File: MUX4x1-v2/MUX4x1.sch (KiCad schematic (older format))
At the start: 14 parts, among them J1 Screw_Terminal_01x02, J2 Conn_01x09_Male, J3 Conn_01x09_Male, J4 Conn_01x09_Male, J5 Conn_01x09_Male, J6 Conn_01x09_Male, J7 Conn_01x03_Male, U1 74LS153, U2 74LS153, U3 74LS153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

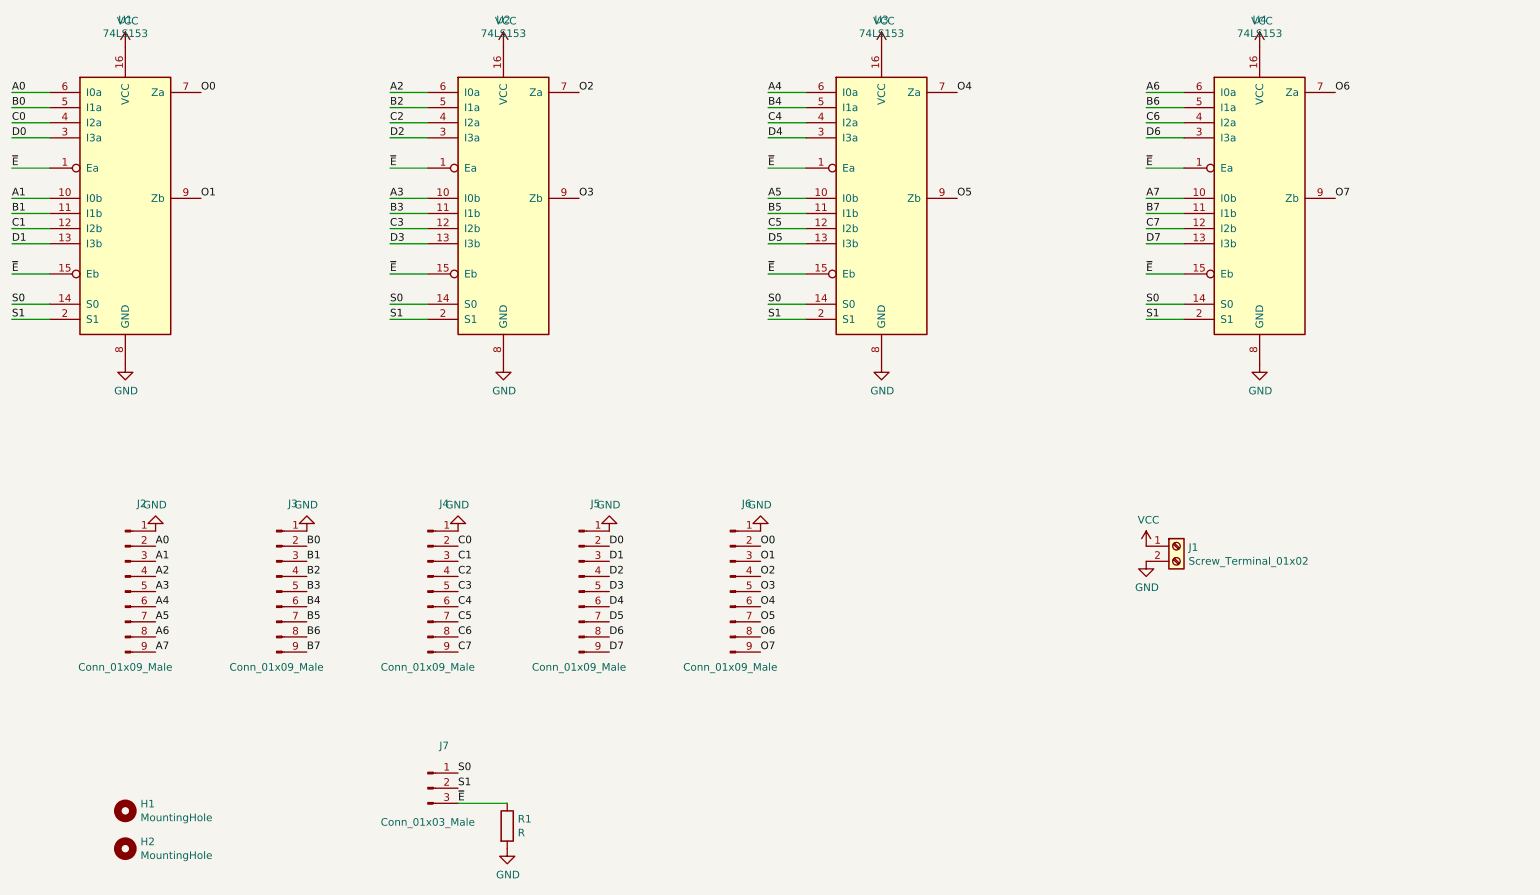
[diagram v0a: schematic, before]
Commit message: We need more sockets!!
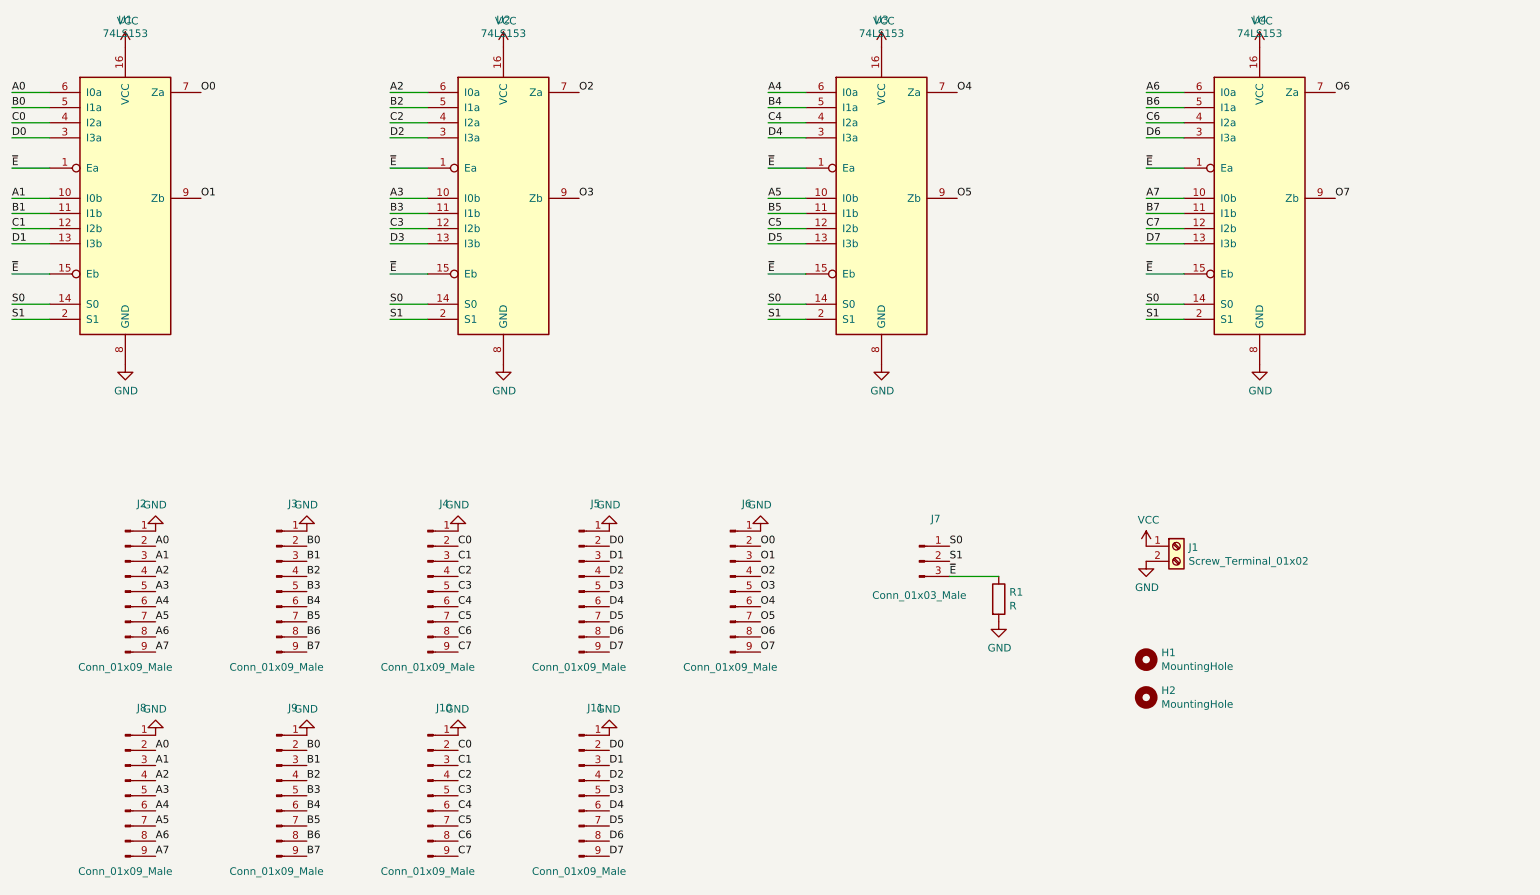
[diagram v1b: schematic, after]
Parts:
- added J10, J11, J8, J9: Conn_01x09_Male, Connector_PinHeader_2.54mm:PinHeader_1x09_P2.54mm_Vertical, symbol Connector:Conn_01x09_Male
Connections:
- net A0: now also J8.2 (Pin_2)
- net A1: now also J8.3 (Pin_3)
- net A2: now also J8.4 (Pin_4)
- net A3: now also J8.5 (Pin_5)
- net A4: now also J8.6 (Pin_6)
- net A5: now also J8.7 (Pin_7)
- net A6: now also J8.8 (Pin_8)
- net A7: now also J8.9 (Pin_9)
- net B0: now also J9.2 (Pin_2)
- net B1: now also J9.3 (Pin_3)
- net B2: now also J9.4 (Pin_4)
- net B3: now also J9.5 (Pin_5)
- net B4: now also J9.6 (Pin_6)
- net B5: now also J9.7 (Pin_7)
- net B6: now also J9.8 (Pin_8)
- net B7: now also J9.9 (Pin_9)
- net C0: now also J10.2 (Pin_2)
- net C1: now also J10.3 (Pin_3)
- net C2: now also J10.4 (Pin_4)
- net C3: now also J10.5 (Pin_5)
- net C4: now also J10.6 (Pin_6)
- net C5: now also J10.7 (Pin_7)
- net C6: now also J10.8 (Pin_8)
- net C7: now also J10.9 (Pin_9)
- net D0: now also J11.2 (Pin_2)
- net D1: now also J11.3 (Pin_3)
- net D2: now also J11.4 (Pin_4)
- net D3: now also J11.5 (Pin_5)
- net D4: now also J11.6 (Pin_6)
- net D5: now also J11.7 (Pin_7)
- net D6: now also J11.8 (Pin_8)
- net D7: now also J11.9 (Pin_9)
- net GND: now also J10.1 (Pin_1), J11.1 (Pin_1), J8.1 (Pin_1), J9.1 (Pin_1)
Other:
- moved on the sheet: H1, H2, J7, R1
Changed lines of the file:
@@
 L Mechanical:MountingHole H1
 U 1 1 62E202A1
-P 2000 6750
-F 0 "H1" H 2100 6796 50  0000 L CNN
-F 1 "MountingHole" H 2100 6705 50  0000 L CNN
-F 2 "MountingHole:MountingHole_3.2mm_M3" H 2000 6750 50  0001 C CNN
-F 3 "~" H 2000 6750 50  0001 C CNN
-	1    2000 6750
+P 8750 5750
+F 0 "H1" H 8850 5796 50  0000 L CNN
+F 1 "MountingHole" H 8850 5705 50  0000 L CNN
+F 2 "MountingHole:MountingHole_3.2mm_M3" H 8750 5750 50  0001 C CNN
+F 3 "~" H 8750 5750 50  0001 C CNN
+	1    8750 5750
 	1    0    0    -1
 $EndComp
@@
 L Mechanical:MountingHole H2
 U 1 1 62E20901
-P 2000 7000
-F 0 "H2" H 2100 7046 50  0000 L CNN
-F 1 "MountingHole" H 2100 6955 50  0000 L CNN
-F 2 "MountingHole:MountingHole_3.2mm_M3" H 2000 7000 50  0001 C CNN
-F 3 "~" H 2000 7000 50  0001 C CNN
-	1    2000 7000
+P 8750 6000
+F 0 "H2" H 8850 6046 50  0000 L CNN
+F 1 "MountingHole" H 8850 5955 50  0000 L CNN
+F 2 "MountingHole:MountingHole_3.2mm_M3" H 8750 6000 50  0001 C CNN
+F 3 "~" H 8750 6000 50  0001 C CNN
+	1    8750 6000
 	1    0    0    -1
 $EndComp
@@
 L Connector:Conn_01x03_Male J7
 U 1 1 62E1D5C5
-P 4000 6600
-F 0 "J7" H 4108 6881 50  0000 C CNN
-F 1 "Conn_01x03_Male" H 4000 6375 50  0000 C CNN
-F 2 "Connector_PinHeader_2.54mm:PinHeader_1x03_P2.54mm_Vertical" H 4000 6600 50  0001 C CNN
-F 3 "~" H 4000 6600 50  0001 C CNN
-	1    4000 6600
-	1    0    0    -1
-$EndComp
-Text Label 4200 6500 0    50   ~ 0
+P 7250 5100
+F 0 "J7" H 7358 5381 50  0000 C CNN
+F 1 "Conn_01x03_Male" H 7250 4875 50  0000 C CNN
+F 2 "Connector_PinHeader_2.54mm:PinHeader_1x03_P2.54mm_Vertical" H 7250 5100 50  0001 C CNN
+F 3 "~" H 7250 5100 50  0001 C CNN
+	1    7250 5100
+	1    0    0    -1
+$EndComp
+Text Label 7450 5000 0    50   ~ 0
 S0
-Text Label 4200 6600 0    50   ~ 0
+Text Label 7450 5100 0    50   ~ 0
 S1
-Text Label 4200 6700 0    50   ~ 0
+Text Label 7450 5200 0    50   ~ 0
 ~E
 $Comp
 L Device:R R1
 U 1 1 62E1F3C7
-P 4525 6850
-F 0 "R1" H 4595 6896 50  0000 L CNN
-F 1 "R" H 4595 6805 50  0000 L CNN
-F 2 "Resistor_SMD:R_0805_2012Metric_Pad1.20x1.40mm_HandSolder" V 4455 6850 50  0001 C CNN
-F 3 "~" H 4525 6850 50  0001 C CNN
-	1    4525 6850
-	1    0    0    -1
-$EndComp
-Wire Wire Line
-	4200 6700 4525 6700
+P 7775 5350
+F 0 "R1" H 7845 5396 50  0000 L CNN
+F 1 "R" H 7845 5305 50  0000 L CNN
+F 2 "Resistor_SMD:R_0805_2012Metric_Pad1.20x1.40mm_HandSolder" V 7705 5350 50  0001 C CNN
+F 3 "~" H 7775 5350 50  0001 C CNN
+	1    7775 5350
+	1    0    0    -1
+$EndComp
+Wire Wire Line
+	7450 5200 7775 5200
 $Comp
 L power:GND #PWR016
 U 1 1 62E205E6
-P 4525 7000
-F 0 "#PWR016" H 4525 6750 50  0001 C CNN
-F 1 "GND" H 4530 6827 50  0000 C CNN
-F 2 "" H 4525 7000 50  0001 C CNN
-F 3 "" H 4525 7000 50  0001 C CNN
-	1    4525 7000
+P 7775 5500
+F 0 "#PWR016" H 7775 5250 50  0001 C CNN
+F 1 "GND" H 7780 5327 50  0000 C CNN
+F 2 "" H 7775 5500 50  0001 C CNN
+F 3 "" H 7775 5500 50  0001 C CNN
+	1    7775 5500
 	1    0    0    -1
 $EndComp
@@
 Text Label 1250 2500 0    50   ~ 0
 ~E
+$Comp
+L Connector:Conn_01x09_Male J8
+U 1 1 62E33207
+P 2000 6650
+F 0 "J8" H 2108 7231 50  0000 C CNN
+F 1 "Conn_01x09_Male" H 2000 6150 50  0000 C CNN
+F 2 "Connector_PinHeader_2.54mm:PinHeader_1x09_P2.54mm_Vertical" H 2000 6650 50  0001 C CNN
+F 3 "~" H 2000 6650 50  0001 C CNN
+	1    2000 6650
+	1    0    0    -1
+$EndComp
+$Comp
+L Connector:Conn_01x09_Male J9
+U 1 1 62E3320D
+P 3000 6650
+F 0 "J9" H 3108 7231 50  0000 C CNN
+F 1 "Conn_01x09_Male" H 3000 6150 50  0000 C CNN
+F 2 "Connector_PinHeader_2.54mm:PinHeader_1x09_P2.54mm_Vertical" H 3000 6650 50  0001 C CNN
+F 3 "~" H 3000 6650 50  0001 C CNN
+	1    3000 6650
+	1    0    0    -1
+$EndComp
+$Comp
+L Connector:Conn_01x09_Male J10
+U 1 1 62E33213
+P 4000 6650
+F 0 "J10" H 4108 7231 50  0000 C CNN
+F 1 "Conn_01x09_Male" H 4000 6150 50  0000 C CNN
+F 2 "Connector_PinHeader_2.54mm:PinHeader_1x09_P2.54mm_Vertical" H 4000 6650 50  0001 C CNN
+F 3 "~" H 4000 6650 50  0001 C CNN
+	1    4000 6650
+	1    0    0    -1
+$EndComp
+$Comp
+L Connector:Conn_01x09_Male J11
+U 1 1 62E33219
+P 5000 6650
+F 0 "J11" H 5108 7231 50  0000 C CNN
+F 1 "Conn_01x09_Male" H 5000 6150 50  0000 C CNN
+F 2 "Connector_PinHeader_2.54mm:PinHeader_1x09_P2.54mm_Vertical" H 5000 6650 50  0001 C CNN
+F 3 "~" H 5000 6650 50  0001 C CNN
+	1    5000 6650
+	1    0    0    -1
+$EndComp
+Text Label 2200 6350 0    50   ~ 0
+A0
+Text Label 2200 6450 0    50   ~ 0
+A1
+Text Label 2200 6550 0    50   ~ 0
+A2
+Text Label 2200 6650 0    50   ~ 0
+A3
+Text Label 2200 6750 0    50   ~ 0
+A4
+Text Label 2200 6850 0    50   ~ 0
+A5
+Text Label 2200 6950 0    50   ~ 0
+A6
+Text Label 2200 7050 0    50   ~ 0
+A7
+$Comp
+L power:GND #PWR0101
+U 1 1 62E33227
+P 2200 6250
+F 0 "#PWR0101" H 2200 6000 50  0001 C CNN
+F 1 "GND" H 2205 6077 50  0000 C CNN
+F 2 "" H 2200 6250 50  0001 C CNN
+F 3 "" H 2200 6250 50  0001 C CNN
+	1    2200 6250
+	-1   0    0    1
+$EndComp
+$Comp
+L power:GND #PWR0102
+U 1 1 62E3322D
+P 3200 6250
+F 0 "#PWR0102" H 3200 6000 50  0001 C CNN
+F 1 "GND" H 3205 6077 50  0000 C CNN
+F 2 "" H 3200 6250 50  0001 C CNN
+F 3 "" H 3200 6250 50  0001 C CNN
+	1    3200 6250
+	-1   0    0    1
+$EndComp
+$Comp
+L power:GND #PWR0103
+U 1 1 62E33233
+P 4200 6250
+F 0 "#PWR0103" H 4200 6000 50  0001 C CNN
+F 1 "GND" H 4205 6077 50  0000 C CNN
+F 2 "" H 4200 6250 50  0001 C CNN
+F 3 "" H 4200 6250 50  0001 C CNN
+	1    4200 6250
+	-1   0    0    1
+$EndComp
+$Comp
+L power:GND #PWR0104
+U 1 1 62E33239
+P 5200 6250
+F 0 "#PWR0104" H 5200 6000 50  0001 C CNN
+F 1 "GND" H 5205 6077 50  0000 C CNN
+F 2 "" H 5200 6250 50  0001 C CNN
+F 3 "" H 5200 6250 50  0001 C CNN
+	1    5200 6250
+	-1   0    0    1
+$EndComp
+Text Label 3200 6350 0    50   ~ 0
+B0
+Text Label 3200 6450 0    50   ~ 0
+B1
+Text Label 3200 6550 0    50   ~ 0
+B2
+Text Label 3200 6650 0    50   ~ 0
+B3
+Text Label 3200 6750 0    50   ~ 0
+B4
+Text Label 3200 6850 0    50   ~ 0
+B5
+Text Label 3200 6950 0    50   ~ 0
+B6
+Text Label 3200 7050 0    50   ~ 0
+B7
+Text Label 4200 6350 0    50   ~ 0
+C0
+Text Label 4200 6450 0    50   ~ 0
+C1
+Text Label 4200 6550 0    50   ~ 0
+C2
+Text Label 4200 6650 0    50   ~ 0
+C3
+Text Label 4200 6750 0    50   ~ 0
+C4
+Text Label 4200 6850 0    50   ~ 0
+C5
+Text Label 4200 6950 0    50   ~ 0
+C6
+Text Label 4200 7050 0    50   ~ 0
+C7
+Text Label 5200 6350 0    50   ~ 0
+D0
+Text Label 5200 6450 0    50   ~ 0
+D1
+Text Label 5200 6550 0    50   ~ 0
+D2
+Text Label 5200 6650 0    50   ~ 0
+D3
+Text Label 5200 6750 0    50   ~ 0
+D4
+Text Label 5200 6850 0    50   ~ 0
+D5
+Text Label 5200 6950 0    50   ~ 0
+D6
+Text Label 5200 7050 0    50   ~ 0
+D7
 $EndSCHEMATC

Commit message: MUX 4:1 PCB is ready
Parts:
- added D1, D2: LED, LED_SMD:LED_0805_2012Metric_Pad1.15x1.40mm_HandSolder, symbol Device:LED
- added R2, R3: 1k, Resistor_SMD:R_0805_2012Metric_Pad1.20x1.40mm_HandSolder, symbol Device:R
- R1: value R -> 10k
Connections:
- net GND: now also D1.1 (K), D2.1 (K)
- net S0: now also R2.2
- net S1: now also R3.2
- new net: D1.2 (A), R2.1
- new net: D2.2 (A), R3.1
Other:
- moved on the sheet: H1, H2, J1
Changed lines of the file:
@@
 U 1 1 62E11506
 P 2000 2700
-F 0 "U1" H 2000 3881 50  0000 C CNN
-F 1 "74LS153" H 2000 3790 50  0000 C CNN
+F 0 "U1" H 2125 3550 50  0000 C CNN
+F 1 "74LS153" H 1775 3550 50  0000 C CNN
 F 2 "Package_DIP:DIP-16_W7.62mm_Socket" H 2000 2700 50  0001 C CNN
 F 3 "http://www.ti.com/lit/gpn/sn74LS153" H 2000 2700 50  0001 C CNN
@@
 U 1 1 62E122CC
 P 4500 2700
-F 0 "U2" H 4500 3881 50  0000 C CNN
-F 1 "74LS153" H 4500 3790 50  0000 C CNN
+F 0 "U2" H 4650 3550 50  0000 C CNN
+F 1 "74LS153" H 4250 3550 50  0000 C CNN
 F 2 "Package_DIP:DIP-16_W7.62mm_Socket" H 4500 2700 50  0001 C CNN
 F 3 "http://www.ti.com/lit/gpn/sn74LS153" H 4500 2700 50  0001 C CNN
@@
 U 1 1 62E1300F
 P 7000 2700
-F 0 "U3" H 7000 3881 50  0000 C CNN
-F 1 "74LS153" H 7000 3790 50  0000 C CNN
+F 0 "U3" H 7175 3550 50  0000 C CNN
+F 1 "74LS153" H 6750 3550 50  0000 C CNN
 F 2 "Package_DIP:DIP-16_W7.62mm_Socket" H 7000 2700 50  0001 C CNN
 F 3 "http://www.ti.com/lit/gpn/sn74LS153" H 7000 2700 50  0001 C CNN
@@
 U 1 1 62E1395C
 P 9500 2700
-F 0 "U4" H 9500 3881 50  0000 C CNN
-F 1 "74LS153" H 9500 3790 50  0000 C CNN
+F 0 "U4" H 9675 3550 50  0000 C CNN
+F 1 "74LS153" H 9250 3550 50  0000 C CNN
 F 2 "Package_DIP:DIP-16_W7.62mm_Socket" H 9500 2700 50  0001 C CNN
 F 3 "http://www.ti.com/lit/gpn/sn74LS153" H 9500 2700 50  0001 C CNN
@@
 L Connector:Screw_Terminal_01x02 J1
 U 1 1 62E1EF2D
-P 8950 5000
-F 0 "J1" H 9030 4992 50  0000 L CNN
-F 1 "Screw_Terminal_01x02" H 9030 4901 50  0000 L CNN
-F 2 "TerminalBlock_Phoenix:TerminalBlock_Phoenix_PT-1,5-2-5.0-H_1x02_P5.00mm_Horizontal" H 8950 5000 50  0001 C CNN
-F 3 "~" H 8950 5000 50  0001 C CNN
-	1    8950 5000
+P 10200 5000
+F 0 "J1" H 10280 4992 50  0000 L CNN
+F 1 "Screw_Terminal_01x02" H 10280 4901 50  0000 L CNN
+F 2 "TerminalBlock_Phoenix:TerminalBlock_Phoenix_PT-1,5-2-5.0-H_1x02_P5.00mm_Horizontal" H 10200 5000 50  0001 C CNN
+F 3 "~" H 10200 5000 50  0001 C CNN
+	1    10200 5000
 	1    0    0    -1
 $EndComp
@@
 L Mechanical:MountingHole H1
 U 1 1 62E202A1
-P 8750 5750
-F 0 "H1" H 8850 5796 50  0000 L CNN
-F 1 "MountingHole" H 8850 5705 50  0000 L CNN
-F 2 "MountingHole:MountingHole_3.2mm_M3" H 8750 5750 50  0001 C CNN
-F 3 "~" H 8750 5750 50  0001 C CNN
-	1    8750 5750
+P 10000 5750
+F 0 "H1" H 10100 5796 50  0000 L CNN
+F 1 "MountingHole" H 10100 5705 50  0000 L CNN
+F 2 "MountingHole:MountingHole_3.2mm_M3" H 10000 5750 50  0001 C CNN
+F 3 "~" H 10000 5750 50  0001 C CNN
+	1    10000 5750
 	1    0    0    -1
 $EndComp
@@
 L Mechanical:MountingHole H2
 U 1 1 62E20901
-P 8750 6000
-F 0 "H2" H 8850 6046 50  0000 L CNN
-F 1 "MountingHole" H 8850 5955 50  0000 L CNN
-F 2 "MountingHole:MountingHole_3.2mm_M3" H 8750 6000 50  0001 C CNN
-F 3 "~" H 8750 6000 50  0001 C CNN
-	1    8750 6000
+P 10000 6000
+F 0 "H2" H 10100 6046 50  0000 L CNN
+F 1 "MountingHole" H 10100 5955 50  0000 L CNN
+F 2 "MountingHole:MountingHole_3.2mm_M3" H 10000 6000 50  0001 C CNN
+F 3 "~" H 10000 6000 50  0001 C CNN
+	1    10000 6000
 	1    0    0    -1
 $EndComp
@@
 L power:VCC #PWR014
 U 1 1 62E45A54
-P 8750 5000
-F 0 "#PWR014" H 8750 4850 50  0001 C CNN
-F 1 "VCC" H 8765 5173 50  0000 C CNN
-F 2 "" H 8750 5000 50  0001 C CNN
-F 3 "" H 8750 5000 50  0001 C CNN
-	1    8750 5000
+P 10000 5000
+F 0 "#PWR014" H 10000 4850 50  0001 C CNN
+F 1 "VCC" H 10015 5173 50  0000 C CNN
+F 2 "" H 10000 5000 50  0001 C CNN
+F 3 "" H 10000 5000 50  0001 C CNN
+	1    10000 5000
 	1    0    0    -1
 $EndComp
@@
 P 9500 1700
 F 0 "#PWR04" H 9500 1550 50  0001 C CNN
-F 1 "VCC" H 9515 1873 50  0000 C CNN
+F 1 "VCC" H 9500 1850 50  0000 C CNN
 F 2 "" H 9500 1700 50  0001 C CNN
 F 3 "" H 9500 1700 50  0001 C CNN
@@
 P 7000 1700
 F 0 "#PWR03" H 7000 1550 50  0001 C CNN
-F 1 "VCC" H 7015 1873 50  0000 C CNN
+F 1 "VCC" H 7000 1850 50  0000 C CNN
 F 2 "" H 7000 1700 50  0001 C CNN
 F 3 "" H 7000 1700 50  0001 C CNN
@@
 P 2000 1700
 F 0 "#PWR01" H 2000 1550 50  0001 C CNN
-F 1 "VCC" H 2015 1873 50  0000 C CNN
+F 1 "VCC" H 2000 1850 50  0000 C CNN
 F 2 "" H 2000 1700 50  0001 C CNN
 F 3 "" H 2000 1700 50  0001 C CNN
@@
 L power:GND #PWR015
 U 1 1 62E47250
-P 8750 5100
-F 0 "#PWR015" H 8750 4850 50  0001 C CNN
-F 1 "GND" H 8755 4927 50  0000 C CNN
-F 2 "" H 8750 5100 50  0001 C CNN
-F 3 "" H 8750 5100 50  0001 C CNN
-	1    8750 5100
+P 10000 5100
+F 0 "#PWR015" H 10000 4850 50  0001 C CNN
+F 1 "GND" H 10005 4927 50  0000 C CNN
+F 2 "" H 10000 5100 50  0001 C CNN
+F 3 "" H 10000 5100 50  0001 C CNN
+	1    10000 5100
 	1    0    0    -1
 $EndComp
@@
 P 7775 5350
 F 0 "R1" H 7845 5396 50  0000 L CNN
-F 1 "R" H 7845 5305 50  0000 L CNN
+F 1 "10k" H 7845 5305 50  0000 L CNN
 F 2 "Resistor_SMD:R_0805_2012Metric_Pad1.20x1.40mm_HandSolder" V 7705 5350 50  0001 C CNN
 F 3 "~" H 7775 5350 50  0001 C CNN
@@
 Text Label 5200 7050 0    50   ~ 0
 D7
+$Comp
+L Device:R R2
+U 1 1 6342CF60
+P 7900 4875
+F 0 "R2" V 7825 4875 50  0000 C CNN
+F 1 "1k" V 7900 4875 50  0000 C CNN
+F 2 "Resistor_SMD:R_0805_2012Metric_Pad1.20x1.40mm_HandSolder" V 7830 4875 50  0001 C CNN
+F 3 "~" H 7900 4875 50  0001 C CNN
+	1    7900 4875
+	0    1    1    0
+$EndComp
+$Comp
+L Device:LED D1
+U 1 1 6342D88F
+P 8200 4875
+F 0 "D1" H 8325 4800 50  0000 C CNN
+F 1 "LED" H 8175 4800 50  0000 C CNN
+F 2 "LED_SMD:LED_0805_2012Metric_Pad1.15x1.40mm_HandSolder" H 8200 4875 50  0001 C CNN
+F 3 "~" H 8200 4875 50  0001 C CNN
+	1    8200 4875
+	-1   0    0    1
+$EndComp
+$Comp
+L Device:R R3
+U 1 1 63439452
+P 7900 5100
+F 0 "R3" V 7825 5100 50  0000 C CNN
+F 1 "1k" V 7900 5100 50  0000 C CNN
+F 2 "Resistor_SMD:R_0805_2012Metric_Pad1.20x1.40mm_HandSolder" V 7830 5100 50  0001 C CNN
+F 3 "~" H 7900 5100 50  0001 C CNN
+	1    7900 5100
+	0    1    1    0
+$EndComp
+$Comp
+L Device:LED D2
+U 1 1 63439458
+P 8200 5100
+F 0 "D2" H 8325 5025 50  0000 C CNN
+F 1 "LED" H 8175 5025 50  0000 C CNN
+F 2 "LED_SMD:LED_0805_2012Metric_Pad1.15x1.40mm_HandSolder" H 8200 5100 50  0001 C CNN
+F 3 "~" H 8200 5100 50  0001 C CNN
+	1    8200 5100
+	-1   0    0    1
+$EndComp
+Wire Wire Line
+	7450 5100 7750 5100
+Wire Wire Line
+	7450 5000 7625 5000
+Wire Wire Line
+	7625 5000 7625 4875
+Wire Wire Line
+	7625 4875 7750 4875
+$Comp
+L power:GND #PWR017
+U 1 1 63441B35
+P 8350 4875
+F 0 "#PWR017" H 8350 4625 50  0001 C CNN
+F 1 "GND" V 8355 4747 50  0000 R CNN
+F 2 "" H 8350 4875 50  0001 C CNN
+F 3 "" H 8350 4875 50  0001 C CNN
+	1    8350 4875
+	0    -1   -1   0
+$EndComp
+$Comp
+L power:GND #PWR018
+U 1 1 63446025
+P 8350 5100
+F 0 "#PWR018" H 8350 4850 50  0001 C CNN
+F 1 "GND" V 8355 4972 50  0000 R CNN
+F 2 "" H 8350 5100 50  0001 C CNN
+F 3 "" H 8350 5100 50  0001 C CNN
+	1    8350 5100
+	0    -1   -1   0
+$EndComp
+$Comp
+L power:PWR_FLAG #FLG0101
+U 1 1 63449476
+P 9500 5300
+F 0 "#FLG0101" H 9500 5375 50  0001 C CNN
+F 1 "PWR_FLAG" H 9500 5473 50  0000 C CNN
+F 2 "" H 9500 5300 50  0001 C CNN
+F 3 "~" H 9500 5300 50  0001 C CNN
+	1    9500 5300
+	1    0    0    -1
+$EndComp
+$Comp
+L power:GND #PWR0105
+U 1 1 63449717
+P 9500 5300
+F 0 "#PWR0105" H 9500 5050 50  0001 C CNN
+F 1 "GND" H 9505 5127 50  0000 C CNN
+F 2 "" H 9500 5300 50  0001 C CNN
+F 3 "" H 9500 5300 50  0001 C CNN
+	1    9500 5300
+	1    0    0    -1
+$EndComp
+$Comp
+L power:PWR_FLAG #FLG0102
+U 1 1 6344BF71
+P 9500 4850
+F 0 "#FLG0102" H 9500 4925 50  0001 C CNN
+F 1 "PWR_FLAG" H 9500 5023 50  0000 C CNN
+F 2 "" H 9500 4850 50  0001 C CNN
+F 3 "~" H 9500 4850 50  0001 C CNN
+	1    9500 4850
+	-1   0    0    1
+$EndComp
+$Comp
+L power:VCC #PWR0106
+U 1 1 6344C7E6
+P 9500 4850
+F 0 "#PWR0106" H 9500 4700 50  0001 C CNN
+F 1 "VCC" H 9515 5023 50  0000 C CNN
+F 2 "" H 9500 4850 50  0001 C CNN
+F 3 "" H 9500 4850 50  0001 C CNN
+	1    9500 4850
+	1    0    0    -1
+$EndComp
 $EndSCHEMATC
